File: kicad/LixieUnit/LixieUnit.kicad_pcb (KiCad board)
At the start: 2 copper layers, 85 x 46 mm, 23 parts, among them P1 CONN_01X10, P2 CONN_01X01, P3 CONN_01X01

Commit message: 表示機のパターンを引き終えた
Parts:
- moved D1 93.9 mm to (140.4, 92.9)
- moved D10 93.9 mm to (140.4, 111.8)
- moved D11 93.9 mm to (160.4, 92.9)
- moved D12 93.9 mm to (160.4, 95.0)
- moved D13 93.9 mm to (160.4, 97.1)
- moved D14 93.9 mm to (160.4, 99.2)
- moved D15 93.9 mm to (160.4, 101.3)
- moved D16 93.9 mm to (160.4, 103.4)
- moved D17 93.9 mm to (160.4, 105.5)
- moved D18 93.9 mm to (160.4, 107.6)
- moved D19 93.9 mm to (160.4, 109.7)
- moved D2 93.9 mm to (140.4, 95.0)
- moved D20 93.9 mm to (160.4, 111.8)
- moved D3 93.9 mm to (140.4, 97.1)
- moved D4 93.9 mm to (140.4, 99.2)
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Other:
- board size 85 x 46 mm -> 24 x 30 mm

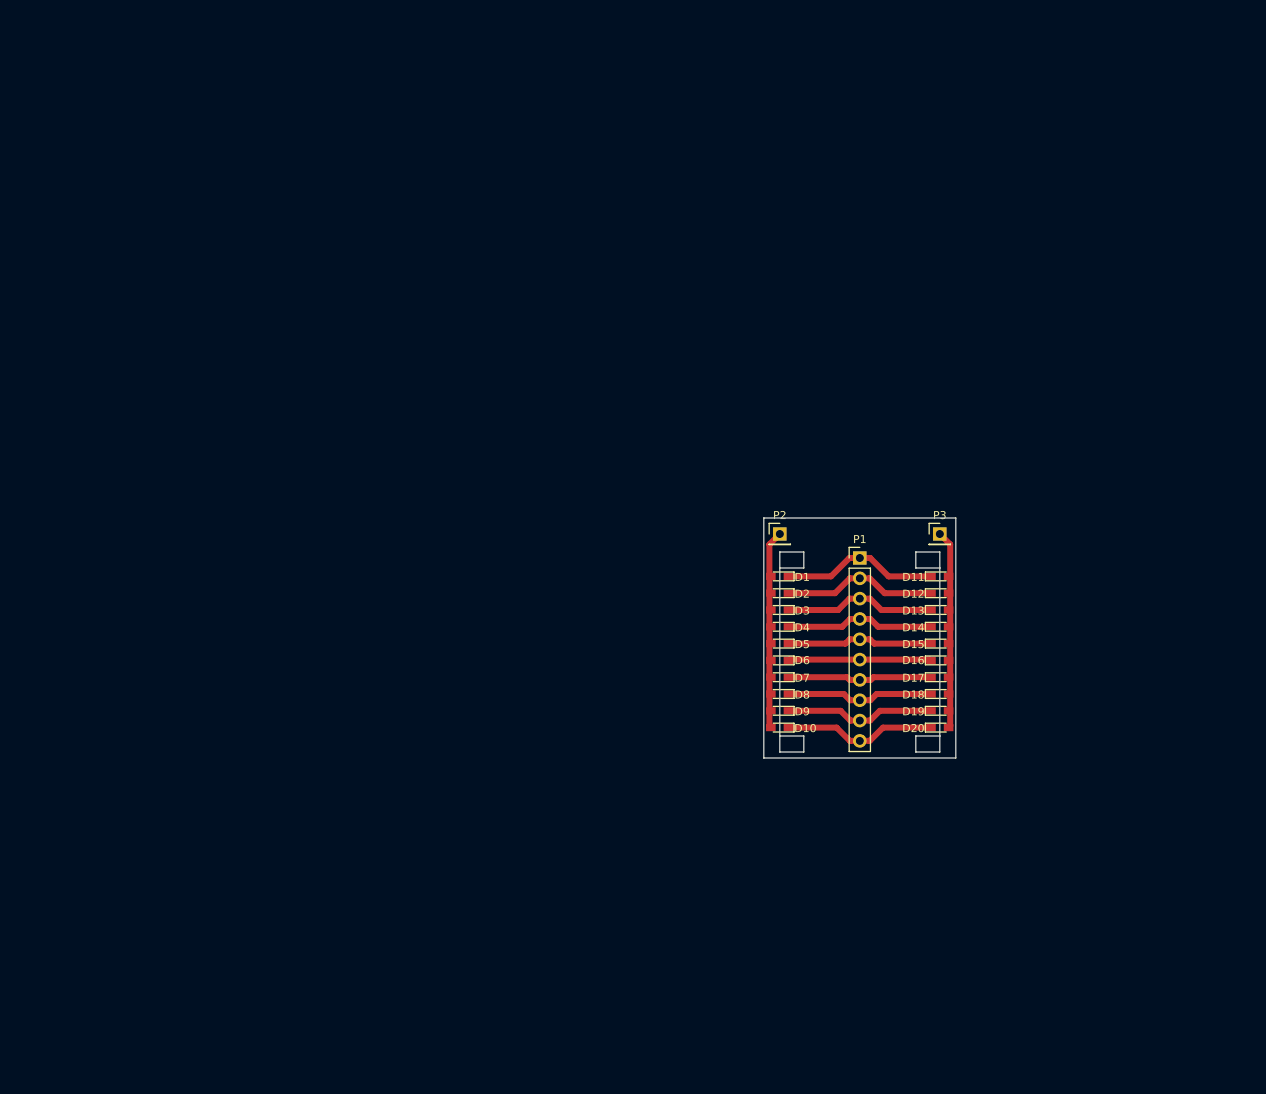
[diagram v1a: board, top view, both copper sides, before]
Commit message: 面付け基板にした。また、面付けの場合、配線が恥から0.4mm以上離れてなければならないので離した。
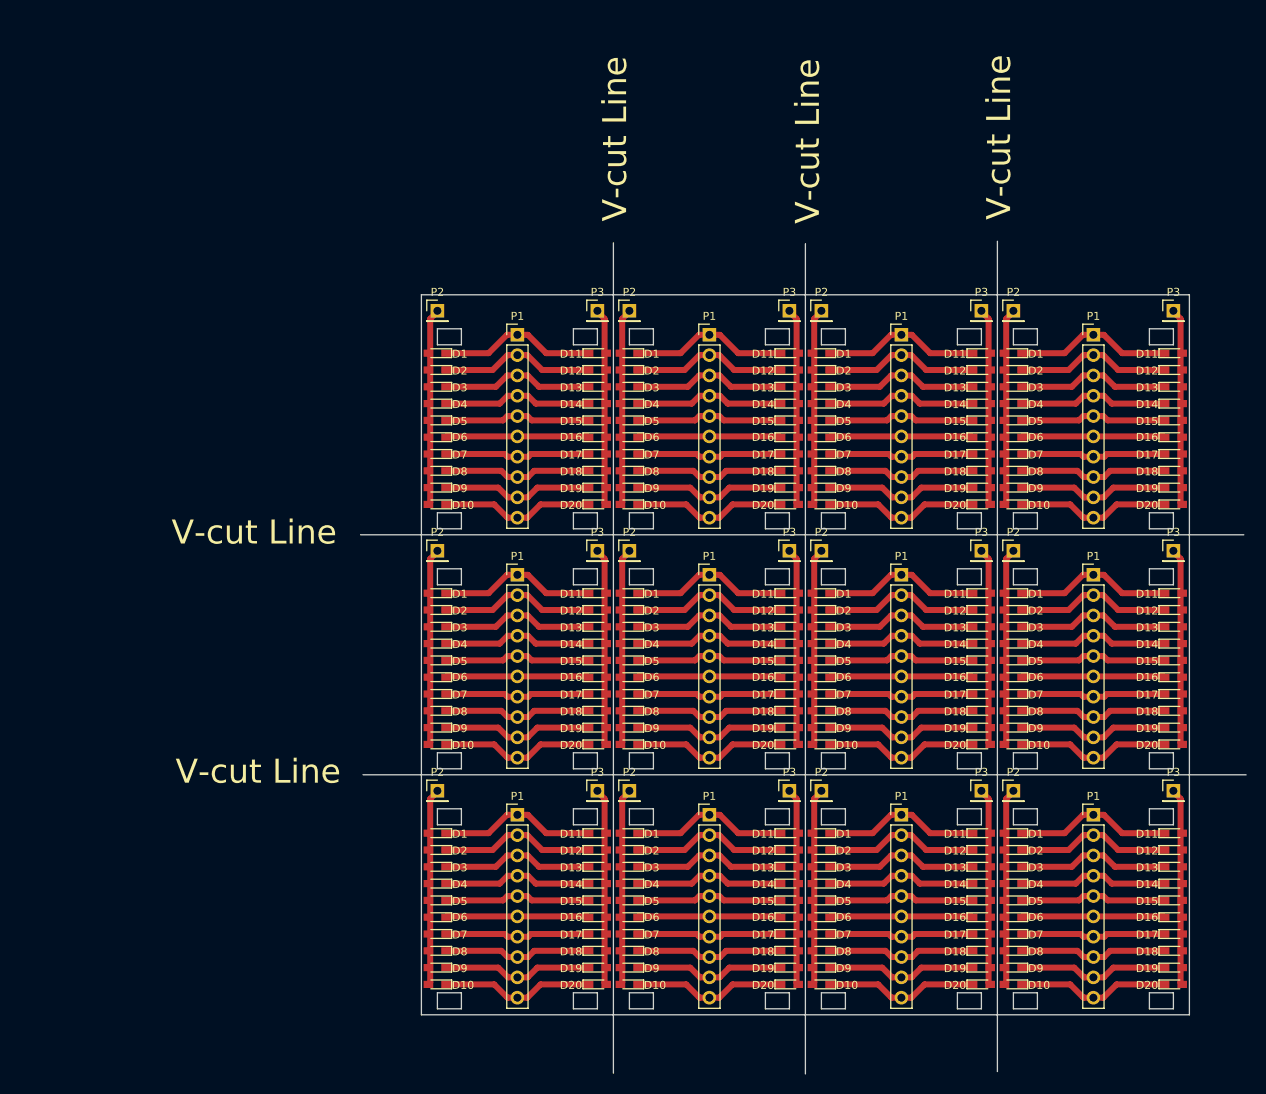
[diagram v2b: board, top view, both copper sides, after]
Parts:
- added D1: Led_Small, LEDs:LED_0603_HandSoldering, F.Cu at (145.6, 125.0)
- added D1: Led_Small, LEDs:LED_0603_HandSoldering, F.Cu at (97.6, 65.0)
- added D1: Led_Small, LEDs:LED_0603_HandSoldering, F.Cu at (97.6, 95.0)
- added D1: Led_Small, LEDs:LED_0603_HandSoldering, F.Cu at (145.6, 95.0)
- added D1: Led_Small, LEDs:LED_0603_HandSoldering, F.Cu at (145.6, 65.0)
- added D1: Led_Small, LEDs:LED_0603_HandSoldering, F.Cu at (169.6, 65.0)
- added D1: Led_Small, LEDs:LED_0603_HandSoldering, F.Cu at (169.6, 95.0)
- added D1: Led_Small, LEDs:LED_0603_HandSoldering, F.Cu at (169.6, 125.0)
- added D1: Led_Small, LEDs:LED_0603_HandSoldering, F.Cu at (121.6, 125.0)
- added D1: Led_Small, LEDs:LED_0603_HandSoldering, F.Cu at (121.6, 95.0)
- added D1: Led_Small, LEDs:LED_0603_HandSoldering, F.Cu at (121.6, 65.0)
- added D10: Led_Small, LEDs:LED_0603_HandSoldering, F.Cu at (145.6, 143.9)
- added D10: Led_Small, LEDs:LED_0603_HandSoldering, F.Cu at (97.6, 83.9)
- added D10: Led_Small, LEDs:LED_0603_HandSoldering, F.Cu at (97.6, 113.9)
- added D10: Led_Small, LEDs:LED_0603_HandSoldering, F.Cu at (145.6, 113.9)
- added D10: Led_Small, LEDs:LED_0603_HandSoldering, F.Cu at (145.6, 83.9)
- added D10: Led_Small, LEDs:LED_0603_HandSoldering, F.Cu at (169.6, 83.9)
- added D10: Led_Small, LEDs:LED_0603_HandSoldering, F.Cu at (169.6, 113.9)
- added D10: Led_Small, LEDs:LED_0603_HandSoldering, F.Cu at (169.6, 143.9)
- added D10: Led_Small, LEDs:LED_0603_HandSoldering, F.Cu at (121.6, 143.9)
- added D10: Led_Small, LEDs:LED_0603_HandSoldering, F.Cu at (121.6, 113.9)
- added D10: Led_Small, LEDs:LED_0603_HandSoldering, F.Cu at (121.6, 83.9)
- added D11: Led_Small, LEDs:LED_0603_HandSoldering, F.Cu at (165.6, 125.0)
- added D11: Led_Small, LEDs:LED_0603_HandSoldering, F.Cu at (117.6, 65.0)
- added D11: Led_Small, LEDs:LED_0603_HandSoldering, F.Cu at (117.6, 95.0)
- added D11: Led_Small, LEDs:LED_0603_HandSoldering, F.Cu at (165.6, 95.0)
- added D11: Led_Small, LEDs:LED_0603_HandSoldering, F.Cu at (165.6, 65.0)
- added D11: Led_Small, LEDs:LED_0603_HandSoldering, F.Cu at (189.6, 65.0)
- added D11: Led_Small, LEDs:LED_0603_HandSoldering, F.Cu at (189.6, 95.0)
- added D11: Led_Small, LEDs:LED_0603_HandSoldering, F.Cu at (189.6, 125.0)
- added D11: Led_Small, LEDs:LED_0603_HandSoldering, F.Cu at (141.6, 125.0)
- added D11: Led_Small, LEDs:LED_0603_HandSoldering, F.Cu at (141.6, 95.0)
- added D11: Led_Small, LEDs:LED_0603_HandSoldering, F.Cu at (141.6, 65.0)
- added D12: Led_Small, LEDs:LED_0603_HandSoldering, F.Cu at (165.6, 127.1)
- added D12: Led_Small, LEDs:LED_0603_HandSoldering, F.Cu at (117.6, 67.1)
- added D12: Led_Small, LEDs:LED_0603_HandSoldering, F.Cu at (117.6, 97.1)
- added D12: Led_Small, LEDs:LED_0603_HandSoldering, F.Cu at (165.6, 97.1)
- added D12: Led_Small, LEDs:LED_0603_HandSoldering, F.Cu at (165.6, 67.1)
- added D12: Led_Small, LEDs:LED_0603_HandSoldering, F.Cu at (189.6, 67.1)
- added D12: Led_Small, LEDs:LED_0603_HandSoldering, F.Cu at (189.6, 97.1)
- added D12: Led_Small, LEDs:LED_0603_HandSoldering, F.Cu at (189.6, 127.1)
- added D12: Led_Small, LEDs:LED_0603_HandSoldering, F.Cu at (141.6, 127.1)
- added D12: Led_Small, LEDs:LED_0603_HandSoldering, F.Cu at (141.6, 97.1)
- added D12: Led_Small, LEDs:LED_0603_HandSoldering, F.Cu at (141.6, 67.1)
- added D13: Led_Small, LEDs:LED_0603_HandSoldering, F.Cu at (165.6, 129.2)
- added D13: Led_Small, LEDs:LED_0603_HandSoldering, F.Cu at (117.6, 69.2)
- added D13: Led_Small, LEDs:LED_0603_HandSoldering, F.Cu at (117.6, 99.2)
- added D13: Led_Small, LEDs:LED_0603_HandSoldering, F.Cu at (165.6, 99.2)
- added D13: Led_Small, LEDs:LED_0603_HandSoldering, F.Cu at (165.6, 69.2)
- added D13: Led_Small, LEDs:LED_0603_HandSoldering, F.Cu at (189.6, 69.2)
- added D13: Led_Small, LEDs:LED_0603_HandSoldering, F.Cu at (189.6, 99.2)
- added D13: Led_Small, LEDs:LED_0603_HandSoldering, F.Cu at (189.6, 129.2)
- added D13: Led_Small, LEDs:LED_0603_HandSoldering, F.Cu at (141.6, 129.2)
- added D13: Led_Small, LEDs:LED_0603_HandSoldering, F.Cu at (141.6, 99.2)
- added D13: Led_Small, LEDs:LED_0603_HandSoldering, F.Cu at (141.6, 69.2)
- added D14: Led_Small, LEDs:LED_0603_HandSoldering, F.Cu at (165.6, 131.3)
- added D14: Led_Small, LEDs:LED_0603_HandSoldering, F.Cu at (117.6, 71.3)
- added D14: Led_Small, LEDs:LED_0603_HandSoldering, F.Cu at (117.6, 101.3)
- added D14: Led_Small, LEDs:LED_0603_HandSoldering, F.Cu at (165.6, 101.3)
- added D14: Led_Small, LEDs:LED_0603_HandSoldering, F.Cu at (165.6, 71.3)
- added D14: Led_Small, LEDs:LED_0603_HandSoldering, F.Cu at (189.6, 71.3)
- added D14: Led_Small, LEDs:LED_0603_HandSoldering, F.Cu at (189.6, 101.3)
- added D14: Led_Small, LEDs:LED_0603_HandSoldering, F.Cu at (189.6, 131.3)
- added D14: Led_Small, LEDs:LED_0603_HandSoldering, F.Cu at (141.6, 131.3)
- added D14: Led_Small, LEDs:LED_0603_HandSoldering, F.Cu at (141.6, 101.3)
- added D14: Led_Small, LEDs:LED_0603_HandSoldering, F.Cu at (141.6, 71.3)
- added D15: Led_Small, LEDs:LED_0603_HandSoldering, F.Cu at (165.6, 133.4)
- added D15: Led_Small, LEDs:LED_0603_HandSoldering, F.Cu at (117.6, 73.4)
- added D15: Led_Small, LEDs:LED_0603_HandSoldering, F.Cu at (117.6, 103.4)
- added D15: Led_Small, LEDs:LED_0603_HandSoldering, F.Cu at (165.6, 103.4)
- added D15: Led_Small, LEDs:LED_0603_HandSoldering, F.Cu at (165.6, 73.4)
- added D15: Led_Small, LEDs:LED_0603_HandSoldering, F.Cu at (189.6, 73.4)
- added D15: Led_Small, LEDs:LED_0603_HandSoldering, F.Cu at (189.6, 103.4)
- added D15: Led_Small, LEDs:LED_0603_HandSoldering, F.Cu at (189.6, 133.4)
- added D15: Led_Small, LEDs:LED_0603_HandSoldering, F.Cu at (141.6, 133.4)
- added D15: Led_Small, LEDs:LED_0603_HandSoldering, F.Cu at (141.6, 103.4)
- added D15: Led_Small, LEDs:LED_0603_HandSoldering, F.Cu at (141.6, 73.4)
- added D16: Led_Small, LEDs:LED_0603_HandSoldering, F.Cu at (165.6, 135.5)
- added D16: Led_Small, LEDs:LED_0603_HandSoldering, F.Cu at (117.6, 75.5)
- added D16: Led_Small, LEDs:LED_0603_HandSoldering, F.Cu at (117.6, 105.5)
- added D16: Led_Small, LEDs:LED_0603_HandSoldering, F.Cu at (165.6, 105.5)
- added D16: Led_Small, LEDs:LED_0603_HandSoldering, F.Cu at (165.6, 75.5)
- added D16: Led_Small, LEDs:LED_0603_HandSoldering, F.Cu at (189.6, 75.5)
- added D16: Led_Small, LEDs:LED_0603_HandSoldering, F.Cu at (189.6, 105.5)
- added D16: Led_Small, LEDs:LED_0603_HandSoldering, F.Cu at (189.6, 135.5)
- added D16: Led_Small, LEDs:LED_0603_HandSoldering, F.Cu at (141.6, 135.5)
- added D16: Led_Small, LEDs:LED_0603_HandSoldering, F.Cu at (141.6, 105.5)
- added D16: Led_Small, LEDs:LED_0603_HandSoldering, F.Cu at (141.6, 75.5)
- added D17: Led_Small, LEDs:LED_0603_HandSoldering, F.Cu at (165.6, 137.6)
- added D17: Led_Small, LEDs:LED_0603_HandSoldering, F.Cu at (117.6, 77.6)
- added D17: Led_Small, LEDs:LED_0603_HandSoldering, F.Cu at (117.6, 107.6)
- added D17: Led_Small, LEDs:LED_0603_HandSoldering, F.Cu at (165.6, 107.6)
- added D17: Led_Small, LEDs:LED_0603_HandSoldering, F.Cu at (165.6, 77.6)
- added D17: Led_Small, LEDs:LED_0603_HandSoldering, F.Cu at (189.6, 77.6)
- added D17: Led_Small, LEDs:LED_0603_HandSoldering, F.Cu at (189.6, 107.6)
- added D17: Led_Small, LEDs:LED_0603_HandSoldering, F.Cu at (189.6, 137.6)
- added D17: Led_Small, LEDs:LED_0603_HandSoldering, F.Cu at (141.6, 137.6)
- added D17: Led_Small, LEDs:LED_0603_HandSoldering, F.Cu at (141.6, 107.6)
- added D17: Led_Small, LEDs:LED_0603_HandSoldering, F.Cu at (141.6, 77.6)
- added D18: Led_Small, LEDs:LED_0603_HandSoldering, F.Cu at (165.6, 139.7)
- added D18: Led_Small, LEDs:LED_0603_HandSoldering, F.Cu at (117.6, 79.7)
- added D18: Led_Small, LEDs:LED_0603_HandSoldering, F.Cu at (117.6, 109.7)
- added D18: Led_Small, LEDs:LED_0603_HandSoldering, F.Cu at (165.6, 109.7)
- added D18: Led_Small, LEDs:LED_0603_HandSoldering, F.Cu at (165.6, 79.7)
- added D18: Led_Small, LEDs:LED_0603_HandSoldering, F.Cu at (189.6, 79.7)
- added D18: Led_Small, LEDs:LED_0603_HandSoldering, F.Cu at (189.6, 109.7)
- added D18: Led_Small, LEDs:LED_0603_HandSoldering, F.Cu at (189.6, 139.7)
- added D18: Led_Small, LEDs:LED_0603_HandSoldering, F.Cu at (141.6, 139.7)
- added D18: Led_Small, LEDs:LED_0603_HandSoldering, F.Cu at (141.6, 109.7)
- added D18: Led_Small, LEDs:LED_0603_HandSoldering, F.Cu at (141.6, 79.7)
- added D19: Led_Small, LEDs:LED_0603_HandSoldering, F.Cu at (165.6, 141.8)
- added D19: Led_Small, LEDs:LED_0603_HandSoldering, F.Cu at (117.6, 81.8)
- added D19: Led_Small, LEDs:LED_0603_HandSoldering, F.Cu at (117.6, 111.8)
- added D19: Led_Small, LEDs:LED_0603_HandSoldering, F.Cu at (165.6, 111.8)
- added D19: Led_Small, LEDs:LED_0603_HandSoldering, F.Cu at (165.6, 81.8)
- added D19: Led_Small, LEDs:LED_0603_HandSoldering, F.Cu at (189.6, 81.8)
- added D19: Led_Small, LEDs:LED_0603_HandSoldering, F.Cu at (189.6, 111.8)
- added D19: Led_Small, LEDs:LED_0603_HandSoldering, F.Cu at (189.6, 141.8)
- added D19: Led_Small, LEDs:LED_0603_HandSoldering, F.Cu at (141.6, 141.8)
- added D19: Led_Small, LEDs:LED_0603_HandSoldering, F.Cu at (141.6, 111.8)
- added D19: Led_Small, LEDs:LED_0603_HandSoldering, F.Cu at (141.6, 81.8)
- added D2: Led_Small, LEDs:LED_0603_HandSoldering, F.Cu at (145.6, 127.1)
- added D2: Led_Small, LEDs:LED_0603_HandSoldering, F.Cu at (97.6, 67.1)
- added D2: Led_Small, LEDs:LED_0603_HandSoldering, F.Cu at (97.6, 97.1)
- added D2: Led_Small, LEDs:LED_0603_HandSoldering, F.Cu at (145.6, 97.1)
- added D2: Led_Small, LEDs:LED_0603_HandSoldering, F.Cu at (145.6, 67.1)
- added D2: Led_Small, LEDs:LED_0603_HandSoldering, F.Cu at (169.6, 67.1)
- added D2: Led_Small, LEDs:LED_0603_HandSoldering, F.Cu at (169.6, 97.1)
- added D2: Led_Small, LEDs:LED_0603_HandSoldering, F.Cu at (169.6, 127.1)
- added D2: Led_Small, LEDs:LED_0603_HandSoldering, F.Cu at (121.6, 127.1)
- added D2: Led_Small, LEDs:LED_0603_HandSoldering, F.Cu at (121.6, 97.1)
- added D2: Led_Small, LEDs:LED_0603_HandSoldering, F.Cu at (121.6, 67.1)
- added D20: Led_Small, LEDs:LED_0603_HandSoldering, F.Cu at (165.6, 143.9)
- added D20: Led_Small, LEDs:LED_0603_HandSoldering, F.Cu at (117.6, 83.9)
- added D20: Led_Small, LEDs:LED_0603_HandSoldering, F.Cu at (117.6, 113.9)
- added D20: Led_Small, LEDs:LED_0603_HandSoldering, F.Cu at (165.6, 113.9)
- added D20: Led_Small, LEDs:LED_0603_HandSoldering, F.Cu at (165.6, 83.9)
- added D20: Led_Small, LEDs:LED_0603_HandSoldering, F.Cu at (189.6, 83.9)
- added D20: Led_Small, LEDs:LED_0603_HandSoldering, F.Cu at (189.6, 113.9)
- added D20: Led_Small, LEDs:LED_0603_HandSoldering, F.Cu at (189.6, 143.9)
- added D20: Led_Small, LEDs:LED_0603_HandSoldering, F.Cu at (141.6, 143.9)
- added D20: Led_Small, LEDs:LED_0603_HandSoldering, F.Cu at (141.6, 113.9)
- added D20: Led_Small, LEDs:LED_0603_HandSoldering, F.Cu at (141.6, 83.9)
- added D3: Led_Small, LEDs:LED_0603_HandSoldering, F.Cu at (145.6, 129.2)
- added D3: Led_Small, LEDs:LED_0603_HandSoldering, F.Cu at (97.6, 69.2)
- added D3: Led_Small, LEDs:LED_0603_HandSoldering, F.Cu at (97.6, 99.2)
- added D3: Led_Small, LEDs:LED_0603_HandSoldering, F.Cu at (145.6, 99.2)
- added D3: Led_Small, LEDs:LED_0603_HandSoldering, F.Cu at (145.6, 69.2)
- added D3: Led_Small, LEDs:LED_0603_HandSoldering, F.Cu at (169.6, 69.2)
- added D3: Led_Small, LEDs:LED_0603_HandSoldering, F.Cu at (169.6, 99.2)
- added D3: Led_Small, LEDs:LED_0603_HandSoldering, F.Cu at (169.6, 129.2)
- added D3: Led_Small, LEDs:LED_0603_HandSoldering, F.Cu at (121.6, 129.2)
- added D3: Led_Small, LEDs:LED_0603_HandSoldering, F.Cu at (121.6, 99.2)
- added D3: Led_Small, LEDs:LED_0603_HandSoldering, F.Cu at (121.6, 69.2)
- added D4: Led_Small, LEDs:LED_0603_HandSoldering, F.Cu at (145.6, 131.3)
- added D4: Led_Small, LEDs:LED_0603_HandSoldering, F.Cu at (97.6, 71.3)
- added D4: Led_Small, LEDs:LED_0603_HandSoldering, F.Cu at (97.6, 101.3)
- added D4: Led_Small, LEDs:LED_0603_HandSoldering, F.Cu at (145.6, 101.3)
- added D4: Led_Small, LEDs:LED_0603_HandSoldering, F.Cu at (145.6, 71.3)
- added D4: Led_Small, LEDs:LED_0603_HandSoldering, F.Cu at (169.6, 71.3)
- added D4: Led_Small, LEDs:LED_0603_HandSoldering, F.Cu at (169.6, 101.3)
- added D4: Led_Small, LEDs:LED_0603_HandSoldering, F.Cu at (169.6, 131.3)
- added D4: Led_Small, LEDs:LED_0603_HandSoldering, F.Cu at (121.6, 131.3)
- added D4: Led_Small, LEDs:LED_0603_HandSoldering, F.Cu at (121.6, 101.3)
- added D4: Led_Small, LEDs:LED_0603_HandSoldering, F.Cu at (121.6, 71.3)
- added D5: Led_Small, LEDs:LED_0603_HandSoldering, F.Cu at (145.6, 133.4)
- added D5: Led_Small, LEDs:LED_0603_HandSoldering, F.Cu at (97.6, 73.4)
- added D5: Led_Small, LEDs:LED_0603_HandSoldering, F.Cu at (97.6, 103.4)
- added D5: Led_Small, LEDs:LED_0603_HandSoldering, F.Cu at (145.6, 103.4)
- added D5: Led_Small, LEDs:LED_0603_HandSoldering, F.Cu at (145.6, 73.4)
- added D5: Led_Small, LEDs:LED_0603_HandSoldering, F.Cu at (169.6, 73.4)
- added D5: Led_Small, LEDs:LED_0603_HandSoldering, F.Cu at (169.6, 103.4)
- added D5: Led_Small, LEDs:LED_0603_HandSoldering, F.Cu at (169.6, 133.4)
- added D5: Led_Small, LEDs:LED_0603_HandSoldering, F.Cu at (121.6, 133.4)
- added D5: Led_Small, LEDs:LED_0603_HandSoldering, F.Cu at (121.6, 103.4)
- added D5: Led_Small, LEDs:LED_0603_HandSoldering, F.Cu at (121.6, 73.4)
- added D6: Led_Small, LEDs:LED_0603_HandSoldering, F.Cu at (145.6, 135.5)
- added D6: Led_Small, LEDs:LED_0603_HandSoldering, F.Cu at (97.6, 75.5)
- added D6: Led_Small, LEDs:LED_0603_HandSoldering, F.Cu at (97.6, 105.5)
- added D6: Led_Small, LEDs:LED_0603_HandSoldering, F.Cu at (145.6, 105.5)
- added D6: Led_Small, LEDs:LED_0603_HandSoldering, F.Cu at (145.6, 75.5)
- added D6: Led_Small, LEDs:LED_0603_HandSoldering, F.Cu at (169.6, 75.5)
- added D6: Led_Small, LEDs:LED_0603_HandSoldering, F.Cu at (169.6, 105.5)
- added D6: Led_Small, LEDs:LED_0603_HandSoldering, F.Cu at (169.6, 135.5)
- added D6: Led_Small, LEDs:LED_0603_HandSoldering, F.Cu at (121.6, 135.5)
- added D6: Led_Small, LEDs:LED_0603_HandSoldering, F.Cu at (121.6, 105.5)
- added D6: Led_Small, LEDs:LED_0603_HandSoldering, F.Cu at (121.6, 75.5)
- added D7: Led_Small, LEDs:LED_0603_HandSoldering, F.Cu at (145.6, 137.6)
- added D7: Led_Small, LEDs:LED_0603_HandSoldering, F.Cu at (97.6, 77.6)
- added D7: Led_Small, LEDs:LED_0603_HandSoldering, F.Cu at (97.6, 107.6)
- added D7: Led_Small, LEDs:LED_0603_HandSoldering, F.Cu at (145.6, 107.6)
- added D7: Led_Small, LEDs:LED_0603_HandSoldering, F.Cu at (145.6, 77.6)
- added D7: Led_Small, LEDs:LED_0603_HandSoldering, F.Cu at (169.6, 77.6)
- added D7: Led_Small, LEDs:LED_0603_HandSoldering, F.Cu at (169.6, 107.6)
- added D7: Led_Small, LEDs:LED_0603_HandSoldering, F.Cu at (169.6, 137.6)
- added D7: Led_Small, LEDs:LED_0603_HandSoldering, F.Cu at (121.6, 137.6)
- added D7: Led_Small, LEDs:LED_0603_HandSoldering, F.Cu at (121.6, 107.6)
- added D7: Led_Small, LEDs:LED_0603_HandSoldering, F.Cu at (121.6, 77.6)
- added D8: Led_Small, LEDs:LED_0603_HandSoldering, F.Cu at (145.6, 139.7)
- added D8: Led_Small, LEDs:LED_0603_HandSoldering, F.Cu at (97.6, 79.7)
- added D8: Led_Small, LEDs:LED_0603_HandSoldering, F.Cu at (97.6, 109.7)
- added D8: Led_Small, LEDs:LED_0603_HandSoldering, F.Cu at (145.6, 109.7)
- added D8: Led_Small, LEDs:LED_0603_HandSoldering, F.Cu at (145.6, 79.7)
- added D8: Led_Small, LEDs:LED_0603_HandSoldering, F.Cu at (169.6, 79.7)
- added D8: Led_Small, LEDs:LED_0603_HandSoldering, F.Cu at (169.6, 109.7)
- added D8: Led_Small, LEDs:LED_0603_HandSoldering, F.Cu at (169.6, 139.7)
- added D8: Led_Small, LEDs:LED_0603_HandSoldering, F.Cu at (121.6, 139.7)
- added D8: Led_Small, LEDs:LED_0603_HandSoldering, F.Cu at (121.6, 109.7)
- added D8: Led_Small, LEDs:LED_0603_HandSoldering, F.Cu at (121.6, 79.7)
- added D9: Led_Small, LEDs:LED_0603_HandSoldering, F.Cu at (145.6, 141.8)
- added D9: Led_Small, LEDs:LED_0603_HandSoldering, F.Cu at (97.6, 81.8)
- added D9: Led_Small, LEDs:LED_0603_HandSoldering, F.Cu at (97.6, 111.8)
- added D9: Led_Small, LEDs:LED_0603_HandSoldering, F.Cu at (145.6, 111.8)
- added D9: Led_Small, LEDs:LED_0603_HandSoldering, F.Cu at (145.6, 81.8)
- added D9: Led_Small, LEDs:LED_0603_HandSoldering, F.Cu at (169.6, 81.8)
- added D9: Led_Small, LEDs:LED_0603_HandSoldering, F.Cu at (169.6, 111.8)
- added D9: Led_Small, LEDs:LED_0603_HandSoldering, F.Cu at (169.6, 141.8)
- added D9: Led_Small, LEDs:LED_0603_HandSoldering, F.Cu at (121.6, 141.8)
- added D9: Led_Small, LEDs:LED_0603_HandSoldering, F.Cu at (121.6, 111.8)
- added D9: Led_Small, LEDs:LED_0603_HandSoldering, F.Cu at (121.6, 81.8)
- added P1: CONN_01X10, Socket_Strips:Socket_Strip_Straight_1x10_Pitch2.54mm, F.Cu at (155.6, 122.7)
- added P1: CONN_01X10, Socket_Strips:Socket_Strip_Straight_1x10_Pitch2.54mm, F.Cu at (107.6, 62.7)
- added P1: CONN_01X10, Socket_Strips:Socket_Strip_Straight_1x10_Pitch2.54mm, F.Cu at (107.6, 92.7)
- added P1: CONN_01X10, Socket_Strips:Socket_Strip_Straight_1x10_Pitch2.54mm, F.Cu at (155.6, 92.7)
- added P1: CONN_01X10, Socket_Strips:Socket_Strip_Straight_1x10_Pitch2.54mm, F.Cu at (155.6, 62.7)
- added P1: CONN_01X10, Socket_Strips:Socket_Strip_Straight_1x10_Pitch2.54mm, F.Cu at (179.6, 62.7)
- added P1: CONN_01X10, Socket_Strips:Socket_Strip_Straight_1x10_Pitch2.54mm, F.Cu at (179.6, 92.7)
- added P1: CONN_01X10, Socket_Strips:Socket_Strip_Straight_1x10_Pitch2.54mm, F.Cu at (179.6, 122.7)
- added P1: CONN_01X10, Socket_Strips:Socket_Strip_Straight_1x10_Pitch2.54mm, F.Cu at (131.6, 122.7)
- added P1: CONN_01X10, Socket_Strips:Socket_Strip_Straight_1x10_Pitch2.54mm, F.Cu at (131.6, 92.7)
- added P1: CONN_01X10, Socket_Strips:Socket_Strip_Straight_1x10_Pitch2.54mm, F.Cu at (131.6, 62.7)
- added P2: CONN_01X01, Socket_Strips:Socket_Strip_Straight_1x01_Pitch2.54mm, F.Cu at (145.6, 119.7)
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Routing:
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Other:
- board size 24 x 30 mm -> 110.7 x 104.1 mm
- board text added: "V-cut Line"

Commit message: 100×100mmのサイズに収めるにはちょっと無理があったので、LixieUnit <-> Mounter <-> MainBoardという3層構造に変更した。
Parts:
- removed the D1 at (145.6, 125.0)
- removed the D1 at (145.6, 95.0)
- removed the D1 at (145.6, 65.0)
- removed the D1 at (169.6, 65.0)
- removed the D1 at (169.6, 95.0)
- removed the D1 at (169.6, 125.0)
- removed the D10 at (145.6, 143.9)
- removed the D10 at (145.6, 113.9)
- removed the D10 at (145.6, 83.9)
- removed the D10 at (169.6, 83.9)
- removed the D10 at (169.6, 113.9)
- removed the D10 at (169.6, 143.9)
- removed the D11 at (165.6, 125.0)
- removed the D11 at (165.6, 95.0)
- removed the D11 at (165.6, 65.0)
- removed the D11 at (189.6, 65.0)
- removed the D11 at (189.6, 95.0)
- removed the D11 at (189.6, 125.0)
- removed the D12 at (165.6, 127.1)
- removed the D12 at (165.6, 97.1)
- removed the D12 at (165.6, 67.1)
- removed the D12 at (189.6, 67.1)
- removed the D12 at (189.6, 97.1)
- removed the D12 at (189.6, 127.1)
- removed the D13 at (165.6, 129.2)
- removed the D13 at (165.6, 99.2)
- removed the D13 at (165.6, 69.2)
- removed the D13 at (189.6, 69.2)
- removed the D13 at (189.6, 99.2)
- removed the D13 at (189.6, 129.2)
- removed the D14 at (165.6, 131.3)
- removed the D14 at (165.6, 101.3)
- removed the D14 at (165.6, 71.3)
- removed the D14 at (189.6, 71.3)
- removed the D14 at (189.6, 101.3)
- removed the D14 at (189.6, 131.3)
- removed the D15 at (165.6, 133.4)
- removed the D15 at (165.6, 103.4)
- removed the D15 at (165.6, 73.4)
- removed the D15 at (189.6, 73.4)
- removed the D15 at (189.6, 103.4)
- removed the D15 at (189.6, 133.4)
- removed the D16 at (165.6, 135.5)
- removed the D16 at (165.6, 105.5)
- removed the D16 at (165.6, 75.5)
- removed the D16 at (189.6, 75.5)
- removed the D16 at (189.6, 105.5)
- removed the D16 at (189.6, 135.5)
- removed the D17 at (165.6, 137.6)
- removed the D17 at (165.6, 107.6)
- removed the D17 at (165.6, 77.6)
- removed the D17 at (189.6, 77.6)
- removed the D17 at (189.6, 107.6)
- removed the D17 at (189.6, 137.6)
- removed the D18 at (165.6, 139.7)
- removed the D18 at (165.6, 109.7)
- removed the D18 at (165.6, 79.7)
- removed the D18 at (189.6, 79.7)
- removed the D18 at (189.6, 109.7)
- removed the D18 at (189.6, 139.7)
- removed the D19 at (165.6, 141.8)
- removed the D19 at (165.6, 111.8)
- removed the D19 at (165.6, 81.8)
- removed the D19 at (189.6, 81.8)
- removed the D19 at (189.6, 111.8)
- removed the D19 at (189.6, 141.8)
- removed the D2 at (145.6, 127.1)
- removed the D2 at (145.6, 97.1)
- removed the D2 at (145.6, 67.1)
- removed the D2 at (169.6, 67.1)
- removed the D2 at (169.6, 97.1)
- removed the D2 at (169.6, 127.1)
- removed the D20 at (165.6, 143.9)
- removed the D20 at (165.6, 113.9)
- removed the D20 at (165.6, 83.9)
- removed the D20 at (189.6, 83.9)
- removed the D20 at (189.6, 113.9)
- removed the D20 at (189.6, 143.9)
- removed the D3 at (145.6, 129.2)
- removed the D3 at (145.6, 99.2)
- removed the D3 at (145.6, 69.2)
- removed the D3 at (169.6, 69.2)
- removed the D3 at (169.6, 99.2)
- removed the D3 at (169.6, 129.2)
- removed the D4 at (145.6, 131.3)
- removed the D4 at (145.6, 101.3)
- removed the D4 at (145.6, 71.3)
- removed the D4 at (169.6, 71.3)
- removed the D4 at (169.6, 101.3)
- removed the D4 at (169.6, 131.3)
- removed the D5 at (145.6, 133.4)
- removed the D5 at (145.6, 103.4)
- removed the D5 at (145.6, 73.4)
- removed the D5 at (169.6, 73.4)
- removed the D5 at (169.6, 103.4)
- removed the D5 at (169.6, 133.4)
- removed the D6 at (145.6, 135.5)
- removed the D6 at (145.6, 105.5)
- removed the D6 at (145.6, 75.5)
- removed the D6 at (169.6, 75.5)
- removed the D6 at (169.6, 105.5)
- removed the D6 at (169.6, 135.5)
- removed the D7 at (145.6, 137.6)
- removed the D7 at (145.6, 107.6)
- removed the D7 at (145.6, 77.6)
- removed the D7 at (169.6, 77.6)
- removed the D7 at (169.6, 107.6)
- removed the D7 at (169.6, 137.6)
- removed the D8 at (145.6, 139.7)
- removed the D8 at (145.6, 109.7)
- removed the D8 at (145.6, 79.7)
- removed the D8 at (169.6, 79.7)
- removed the D8 at (169.6, 109.7)
- removed the D8 at (169.6, 139.7)
- removed the D9 at (145.6, 141.8)
- removed the D9 at (145.6, 111.8)
- removed the D9 at (145.6, 81.8)
- removed the D9 at (169.6, 81.8)
- removed the D9 at (169.6, 111.8)
- removed the D9 at (169.6, 141.8)
- removed the P1 at (155.6, 122.7)
- removed the P1 at (155.6, 92.7)
- removed the P1 at (155.6, 62.7)
- removed the P1 at (179.6, 62.7)
- removed the P1 at (179.6, 92.7)
- removed the P1 at (179.6, 122.7)
- removed the P2 at (145.6, 119.7)
- removed the P2 at (97.6, 59.7)
- removed the P2 at (97.6, 89.7)
- removed the P2 at (145.6, 89.7)
- removed the P2 at (145.6, 59.7)
- removed the P2 at (169.6, 59.7)
- removed the P2 at (169.6, 89.7)
- removed the P2 at (169.6, 119.7)
- removed the P2 at (121.6, 119.7)
- removed the P2 at (121.6, 89.7)
- removed the P2 at (121.6, 59.7)
- removed the P3 at (165.6, 119.7)
- removed the P3 at (117.6, 59.7)
- removed the P3 at (117.6, 89.7)
- removed the P3 at (165.6, 89.7)
- removed the P3 at (165.6, 59.7)
- removed the P3 at (189.6, 59.7)
- removed the P3 at (189.6, 89.7)
- removed the P3 at (189.6, 119.7)
- removed the P3 at (141.6, 119.7)
- removed the P3 at (141.6, 89.7)
- removed the P3 at (141.6, 59.7)
- added D1: Led_Small, LEDs:LED_0603_HandSoldering, F.Cu at (169.7, 65.0)
- added D1: Led_Small, LEDs:LED_0603_HandSoldering, F.Cu at (169.7, 95.0)
- added D1: Led_Small, LEDs:LED_0603_HandSoldering, F.Cu at (169.7, 125.0)
- added D1: Led_Small, LEDs:LED_0603_HandSoldering, F.Cu at (145.6, 125.0)
- added D1: Led_Small, LEDs:LED_0603_HandSoldering, F.Cu at (145.6, 95.0)
- added D1: Led_Small, LEDs:LED_0603_HandSoldering, F.Cu at (145.6, 65.0)
- added D10: Led_Small, LEDs:LED_0603_HandSoldering, F.Cu at (169.7, 83.9)
- added D10: Led_Small, LEDs:LED_0603_HandSoldering, F.Cu at (169.7, 113.9)
- added D10: Led_Small, LEDs:LED_0603_HandSoldering, F.Cu at (169.7, 143.9)
- added D10: Led_Small, LEDs:LED_0603_HandSoldering, F.Cu at (145.6, 143.9)
- added D10: Led_Small, LEDs:LED_0603_HandSoldering, F.Cu at (145.6, 113.9)
- added D10: Led_Small, LEDs:LED_0603_HandSoldering, F.Cu at (145.6, 83.9)
- added D11: Led_Small, LEDs:LED_0603_HandSoldering, F.Cu at (189.7, 65.0)
- added D11: Led_Small, LEDs:LED_0603_HandSoldering, F.Cu at (189.7, 95.0)
- added D11: Led_Small, LEDs:LED_0603_HandSoldering, F.Cu at (189.7, 125.0)
- added D11: Led_Small, LEDs:LED_0603_HandSoldering, F.Cu at (165.7, 125.0)
- added D11: Led_Small, LEDs:LED_0603_HandSoldering, F.Cu at (165.7, 95.0)
- added D11: Led_Small, LEDs:LED_0603_HandSoldering, F.Cu at (165.7, 65.0)
- added D12: Led_Small, LEDs:LED_0603_HandSoldering, F.Cu at (189.7, 67.1)
- added D12: Led_Small, LEDs:LED_0603_HandSoldering, F.Cu at (189.7, 97.1)
- added D12: Led_Small, LEDs:LED_0603_HandSoldering, F.Cu at (189.7, 127.1)
- added D12: Led_Small, LEDs:LED_0603_HandSoldering, F.Cu at (165.7, 127.1)
- added D12: Led_Small, LEDs:LED_0603_HandSoldering, F.Cu at (165.7, 97.1)
- added D12: Led_Small, LEDs:LED_0603_HandSoldering, F.Cu at (165.7, 67.1)
- added D13: Led_Small, LEDs:LED_0603_HandSoldering, F.Cu at (189.7, 69.2)
- added D13: Led_Small, LEDs:LED_0603_HandSoldering, F.Cu at (189.7, 99.2)
- added D13: Led_Small, LEDs:LED_0603_HandSoldering, F.Cu at (189.7, 129.2)
- added D13: Led_Small, LEDs:LED_0603_HandSoldering, F.Cu at (165.7, 129.2)
- added D13: Led_Small, LEDs:LED_0603_HandSoldering, F.Cu at (165.7, 99.2)
- added D13: Led_Small, LEDs:LED_0603_HandSoldering, F.Cu at (165.7, 69.2)
- added D14: Led_Small, LEDs:LED_0603_HandSoldering, F.Cu at (189.7, 71.3)
- added D14: Led_Small, LEDs:LED_0603_HandSoldering, F.Cu at (189.7, 101.3)
- added D14: Led_Small, LEDs:LED_0603_HandSoldering, F.Cu at (189.7, 131.3)
- added D14: Led_Small, LEDs:LED_0603_HandSoldering, F.Cu at (165.7, 131.3)
- added D14: Led_Small, LEDs:LED_0603_HandSoldering, F.Cu at (165.7, 101.3)
- added D14: Led_Small, LEDs:LED_0603_HandSoldering, F.Cu at (165.7, 71.3)
- added D15: Led_Small, LEDs:LED_0603_HandSoldering, F.Cu at (189.7, 73.4)
- added D15: Led_Small, LEDs:LED_0603_HandSoldering, F.Cu at (189.7, 103.4)
- added D15: Led_Small, LEDs:LED_0603_HandSoldering, F.Cu at (189.7, 133.4)
- added D15: Led_Small, LEDs:LED_0603_HandSoldering, F.Cu at (165.7, 133.4)
- added D15: Led_Small, LEDs:LED_0603_HandSoldering, F.Cu at (165.7, 103.4)
- added D15: Led_Small, LEDs:LED_0603_HandSoldering, F.Cu at (165.7, 73.4)
- added D16: Led_Small, LEDs:LED_0603_HandSoldering, F.Cu at (189.7, 75.5)
- added D16: Led_Small, LEDs:LED_0603_HandSoldering, F.Cu at (189.7, 105.5)
- added D16: Led_Small, LEDs:LED_0603_HandSoldering, F.Cu at (189.7, 135.5)
- added D16: Led_Small, LEDs:LED_0603_HandSoldering, F.Cu at (165.7, 135.5)
- added D16: Led_Small, LEDs:LED_0603_HandSoldering, F.Cu at (165.7, 105.5)
- added D16: Led_Small, LEDs:LED_0603_HandSoldering, F.Cu at (165.7, 75.5)
- added D17: Led_Small, LEDs:LED_0603_HandSoldering, F.Cu at (189.7, 77.6)
- added D17: Led_Small, LEDs:LED_0603_HandSoldering, F.Cu at (189.7, 107.6)
- added D17: Led_Small, LEDs:LED_0603_HandSoldering, F.Cu at (189.7, 137.6)
- added D17: Led_Small, LEDs:LED_0603_HandSoldering, F.Cu at (165.7, 137.6)
- added D17: Led_Small, LEDs:LED_0603_HandSoldering, F.Cu at (165.7, 107.6)
- added D17: Led_Small, LEDs:LED_0603_HandSoldering, F.Cu at (165.7, 77.6)
- added D18: Led_Small, LEDs:LED_0603_HandSoldering, F.Cu at (189.7, 79.7)
- added D18: Led_Small, LEDs:LED_0603_HandSoldering, F.Cu at (189.7, 109.7)
- added D18: Led_Small, LEDs:LED_0603_HandSoldering, F.Cu at (189.7, 139.7)
- added D18: Led_Small, LEDs:LED_0603_HandSoldering, F.Cu at (165.7, 139.7)
- added D18: Led_Small, LEDs:LED_0603_HandSoldering, F.Cu at (165.7, 109.7)
- added D18: Led_Small, LEDs:LED_0603_HandSoldering, F.Cu at (165.7, 79.7)
- added D19: Led_Small, LEDs:LED_0603_HandSoldering, F.Cu at (189.7, 81.8)
- added D19: Led_Small, LEDs:LED_0603_HandSoldering, F.Cu at (189.7, 111.8)
- added D19: Led_Small, LEDs:LED_0603_HandSoldering, F.Cu at (189.7, 141.8)
- added D19: Led_Small, LEDs:LED_0603_HandSoldering, F.Cu at (165.7, 141.8)
- added D19: Led_Small, LEDs:LED_0603_HandSoldering, F.Cu at (165.7, 111.8)
- added D19: Led_Small, LEDs:LED_0603_HandSoldering, F.Cu at (165.7, 81.8)
- added D2: Led_Small, LEDs:LED_0603_HandSoldering, F.Cu at (169.7, 67.1)
- added D2: Led_Small, LEDs:LED_0603_HandSoldering, F.Cu at (169.7, 97.1)
- added D2: Led_Small, LEDs:LED_0603_HandSoldering, F.Cu at (169.7, 127.1)
- added D2: Led_Small, LEDs:LED_0603_HandSoldering, F.Cu at (145.6, 127.1)
- added D2: Led_Small, LEDs:LED_0603_HandSoldering, F.Cu at (145.6, 97.1)
- added D2: Led_Small, LEDs:LED_0603_HandSoldering, F.Cu at (145.6, 67.1)
- added D20: Led_Small, LEDs:LED_0603_HandSoldering, F.Cu at (189.7, 83.9)
- added D20: Led_Small, LEDs:LED_0603_HandSoldering, F.Cu at (189.7, 113.9)
- added D20: Led_Small, LEDs:LED_0603_HandSoldering, F.Cu at (189.7, 143.9)
- added D20: Led_Small, LEDs:LED_0603_HandSoldering, F.Cu at (165.7, 143.9)
- added D20: Led_Small, LEDs:LED_0603_HandSoldering, F.Cu at (165.7, 113.9)
- added D20: Led_Small, LEDs:LED_0603_HandSoldering, F.Cu at (165.7, 83.9)
- added D3: Led_Small, LEDs:LED_0603_HandSoldering, F.Cu at (169.7, 69.2)
- added D3: Led_Small, LEDs:LED_0603_HandSoldering, F.Cu at (169.7, 99.2)
- added D3: Led_Small, LEDs:LED_0603_HandSoldering, F.Cu at (169.7, 129.2)
- added D3: Led_Small, LEDs:LED_0603_HandSoldering, F.Cu at (145.6, 129.2)
- added D3: Led_Small, LEDs:LED_0603_HandSoldering, F.Cu at (145.6, 99.2)
- added D3: Led_Small, LEDs:LED_0603_HandSoldering, F.Cu at (145.6, 69.2)
- added D4: Led_Small, LEDs:LED_0603_HandSoldering, F.Cu at (169.7, 71.3)
- added D4: Led_Small, LEDs:LED_0603_HandSoldering, F.Cu at (169.7, 101.3)
- added D4: Led_Small, LEDs:LED_0603_HandSoldering, F.Cu at (169.7, 131.3)
- added D4: Led_Small, LEDs:LED_0603_HandSoldering, F.Cu at (145.6, 131.3)
- added D4: Led_Small, LEDs:LED_0603_HandSoldering, F.Cu at (145.6, 101.3)
- added D4: Led_Small, LEDs:LED_0603_HandSoldering, F.Cu at (145.6, 71.3)
- added D5: Led_Small, LEDs:LED_0603_HandSoldering, F.Cu at (169.7, 73.4)
- added D5: Led_Small, LEDs:LED_0603_HandSoldering, F.Cu at (169.7, 103.4)
- added D5: Led_Small, LEDs:LED_0603_HandSoldering, F.Cu at (169.7, 133.4)
- added D5: Led_Small, LEDs:LED_0603_HandSoldering, F.Cu at (145.6, 133.4)
- added D5: Led_Small, LEDs:LED_0603_HandSoldering, F.Cu at (145.6, 103.4)
- added D5: Led_Small, LEDs:LED_0603_HandSoldering, F.Cu at (145.6, 73.4)
- added D6: Led_Small, LEDs:LED_0603_HandSoldering, F.Cu at (169.7, 75.5)
- added D6: Led_Small, LEDs:LED_0603_HandSoldering, F.Cu at (169.7, 105.5)
- added D6: Led_Small, LEDs:LED_0603_HandSoldering, F.Cu at (169.7, 135.5)
- added D6: Led_Small, LEDs:LED_0603_HandSoldering, F.Cu at (145.6, 135.5)
- added D6: Led_Small, LEDs:LED_0603_HandSoldering, F.Cu at (145.6, 105.5)
- added D6: Led_Small, LEDs:LED_0603_HandSoldering, F.Cu at (145.6, 75.5)
- added D7: Led_Small, LEDs:LED_0603_HandSoldering, F.Cu at (169.7, 77.6)
- added D7: Led_Small, LEDs:LED_0603_HandSoldering, F.Cu at (169.7, 107.6)
- added D7: Led_Small, LEDs:LED_0603_HandSoldering, F.Cu at (169.7, 137.6)
- added D7: Led_Small, LEDs:LED_0603_HandSoldering, F.Cu at (145.6, 137.6)
- added D7: Led_Small, LEDs:LED_0603_HandSoldering, F.Cu at (145.6, 107.6)
- added D7: Led_Small, LEDs:LED_0603_HandSoldering, F.Cu at (145.6, 77.6)
- added D8: Led_Small, LEDs:LED_0603_HandSoldering, F.Cu at (169.7, 79.7)
- added D8: Led_Small, LEDs:LED_0603_HandSoldering, F.Cu at (169.7, 109.7)
- added D8: Led_Small, LEDs:LED_0603_HandSoldering, F.Cu at (169.7, 139.7)
- added D8: Led_Small, LEDs:LED_0603_HandSoldering, F.Cu at (145.6, 139.7)
- added D8: Led_Small, LEDs:LED_0603_HandSoldering, F.Cu at (145.6, 109.7)
- added D8: Led_Small, LEDs:LED_0603_HandSoldering, F.Cu at (145.6, 79.7)
- added D9: Led_Small, LEDs:LED_0603_HandSoldering, F.Cu at (169.7, 81.8)
- added D9: Led_Small, LEDs:LED_0603_HandSoldering, F.Cu at (169.7, 111.8)
- added D9: Led_Small, LEDs:LED_0603_HandSoldering, F.Cu at (169.7, 141.8)
- added D9: Led_Small, LEDs:LED_0603_HandSoldering, F.Cu at (145.6, 141.8)
- added D9: Led_Small, LEDs:LED_0603_HandSoldering, F.Cu at (145.6, 111.8)
- added D9: Led_Small, LEDs:LED_0603_HandSoldering, F.Cu at (145.6, 81.8)
- added P1: CONN_01X10, Socket_Strips:Socket_Strip_Straight_1x10_Pitch2.54mm, F.Cu at (179.7, 62.7)
- added P1: CONN_01X10, Socket_Strips:Socket_Strip_Straight_1x10_Pitch2.54mm, F.Cu at (179.7, 92.7)
- added P1: CONN_01X10, Socket_Strips:Socket_Strip_Straight_1x10_Pitch2.54mm, F.Cu at (179.7, 122.7)
- added P1: CONN_01X10, Socket_Strips:Socket_Strip_Straight_1x10_Pitch2.54mm, F.Cu at (155.7, 122.7)
- added P1: CONN_01X10, Socket_Strips:Socket_Strip_Straight_1x10_Pitch2.54mm, F.Cu at (155.7, 92.7)
- added P1: CONN_01X10, Socket_Strips:Socket_Strip_Straight_1x10_Pitch2.54mm, F.Cu at (155.7, 62.7)
- added P2: CONN_01X01, Socket_Strips:Socket_Strip_Straight_1x01_Pitch2.54mm, F.Cu at (177.9, 59.5)
- added P2: CONN_01X01, Socket_Strips:Socket_Strip_Straight_1x01_Pitch2.54mm, F.Cu at (105.8, 59.5)
- added P2: CONN_01X01, Socket_Strips:Socket_Strip_Straight_1x01_Pitch2.54mm, F.Cu at (105.8, 89.5)
- added P2: CONN_01X01, Socket_Strips:Socket_Strip_Straight_1x01_Pitch2.54mm, F.Cu at (177.9, 89.5)
- added P2: CONN_01X01, Socket_Strips:Socket_Strip_Straight_1x01_Pitch2.54mm, F.Cu at (177.9, 119.5)
- added P2: CONN_01X01, Socket_Strips:Socket_Strip_Straight_1x01_Pitch2.54mm, F.Cu at (129.8, 59.5)
- added P2: CONN_01X01, Socket_Strips:Socket_Strip_Straight_1x01_Pitch2.54mm, F.Cu at (129.8, 89.5)
- added P2: CONN_01X01, Socket_Strips:Socket_Strip_Straight_1x01_Pitch2.54mm, F.Cu at (129.8, 119.5)
- added P2: CONN_01X01, Socket_Strips:Socket_Strip_Straight_1x01_Pitch2.54mm, F.Cu at (153.8, 119.5)
- added P2: CONN_01X01, Socket_Strips:Socket_Strip_Straight_1x01_Pitch2.54mm, F.Cu at (153.8, 89.5)
- added P2: CONN_01X01, Socket_Strips:Socket_Strip_Straight_1x01_Pitch2.54mm, F.Cu at (153.8, 59.5)
- added P3: CONN_01X01, Socket_Strips:Socket_Strip_Straight_1x01_Pitch2.54mm, F.Cu at (181.5, 59.5)
- added P3: CONN_01X01, Socket_Strips:Socket_Strip_Straight_1x01_Pitch2.54mm, F.Cu at (109.4, 59.5)
- added P3: CONN_01X01, Socket_Strips:Socket_Strip_Straight_1x01_Pitch2.54mm, F.Cu at (109.4, 89.5)
- added P3: CONN_01X01, Socket_Strips:Socket_Strip_Straight_1x01_Pitch2.54mm, F.Cu at (181.5, 89.5)
- added P3: CONN_01X01, Socket_Strips:Socket_Strip_Straight_1x01_Pitch2.54mm, F.Cu at (181.5, 119.5)
- added P3: CONN_01X01, Socket_Strips:Socket_Strip_Straight_1x01_Pitch2.54mm, F.Cu at (133.4, 59.5)
- added P3: CONN_01X01, Socket_Strips:Socket_Strip_Straight_1x01_Pitch2.54mm, F.Cu at (133.4, 89.5)
- added P3: CONN_01X01, Socket_Strips:Socket_Strip_Straight_1x01_Pitch2.54mm, F.Cu at (133.4, 119.5)
- added P3: CONN_01X01, Socket_Strips:Socket_Strip_Straight_1x01_Pitch2.54mm, F.Cu at (157.4, 119.5)
- added P3: CONN_01X01, Socket_Strips:Socket_Strip_Straight_1x01_Pitch2.54mm, F.Cu at (157.4, 89.5)
- added P3: CONN_01X01, Socket_Strips:Socket_Strip_Straight_1x01_Pitch2.54mm, F.Cu at (157.4, 59.5)
- moved P2 8.20 mm to (105.8, 119.5)
- moved P3 8.20 mm to (109.4, 119.5)
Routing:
- net Net-(D11-Pad2): track 295.9 -> 395.8 mm
- net Net-(D1-Pad2): track 296.0 -> 394.7 mm
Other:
- board size 110.7 x 104.1 mm -> 111 x 104.3 mm
